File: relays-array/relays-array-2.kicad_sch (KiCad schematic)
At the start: 28 parts, among them J1 NMJ6HCD2, J10 Screw_Terminal_01x02, J14 NMJ6HCD2, J15 Screw_Terminal_01x02, J2 NMJ6HCD2, J3 Screw_Terminal_01x02, K1 G2RL-2, K2 G2RL-2, U1 OPA134

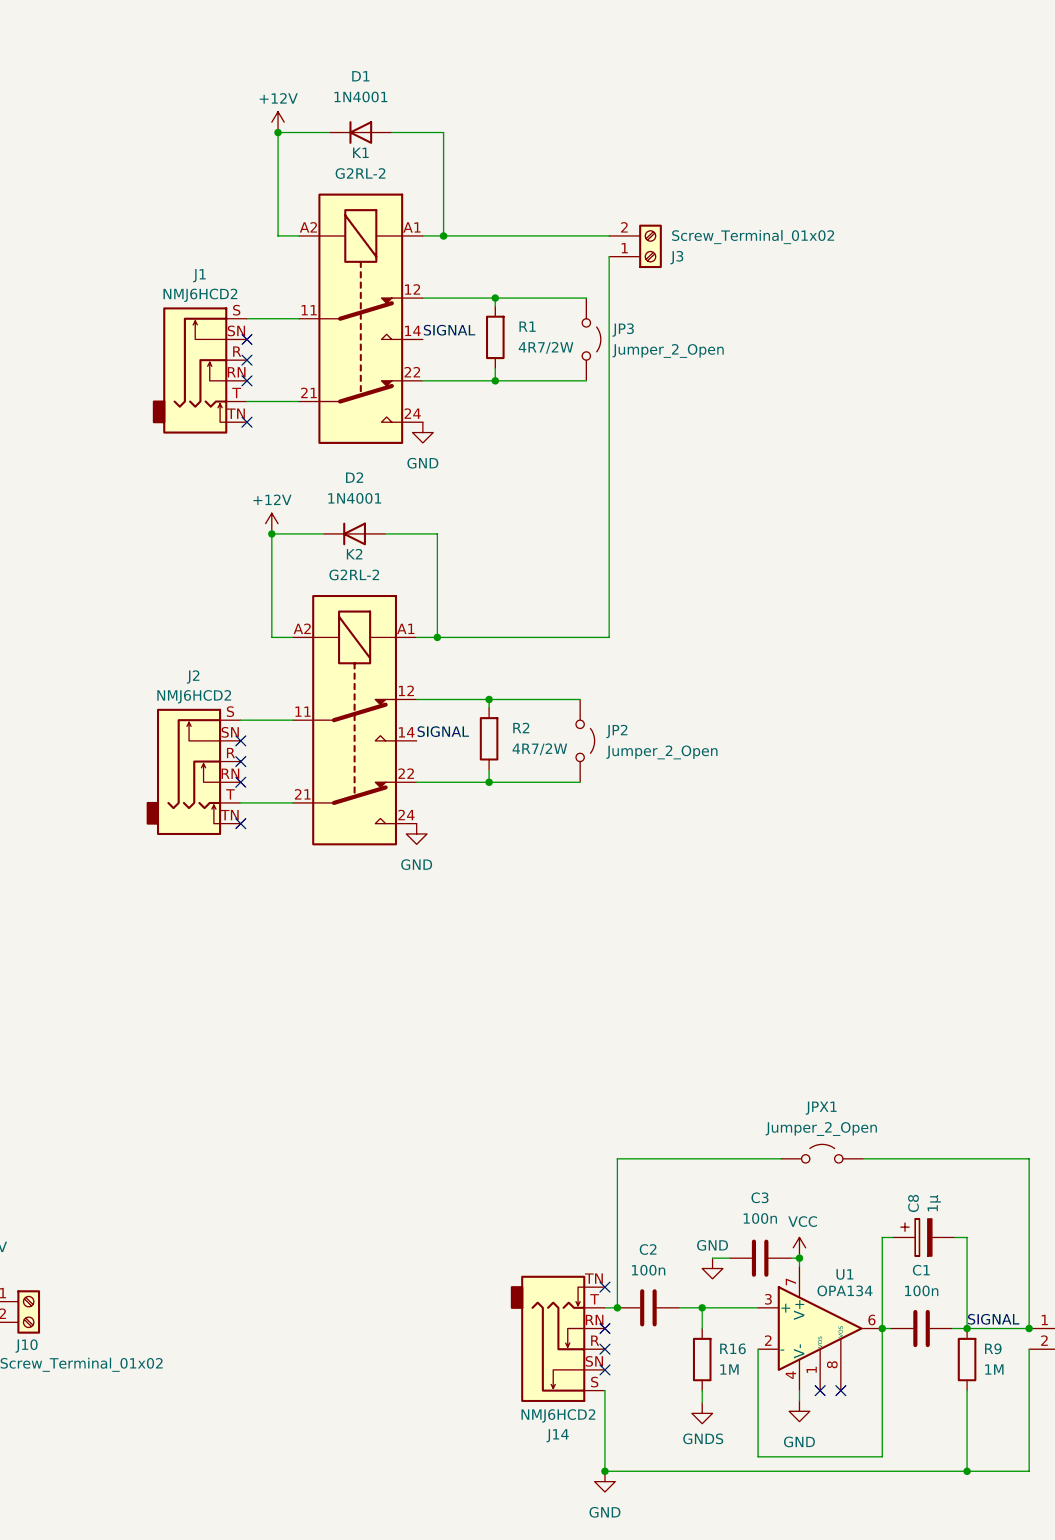
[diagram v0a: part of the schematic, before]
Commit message: relays-array: add terminal block for buffer use w/ external connector
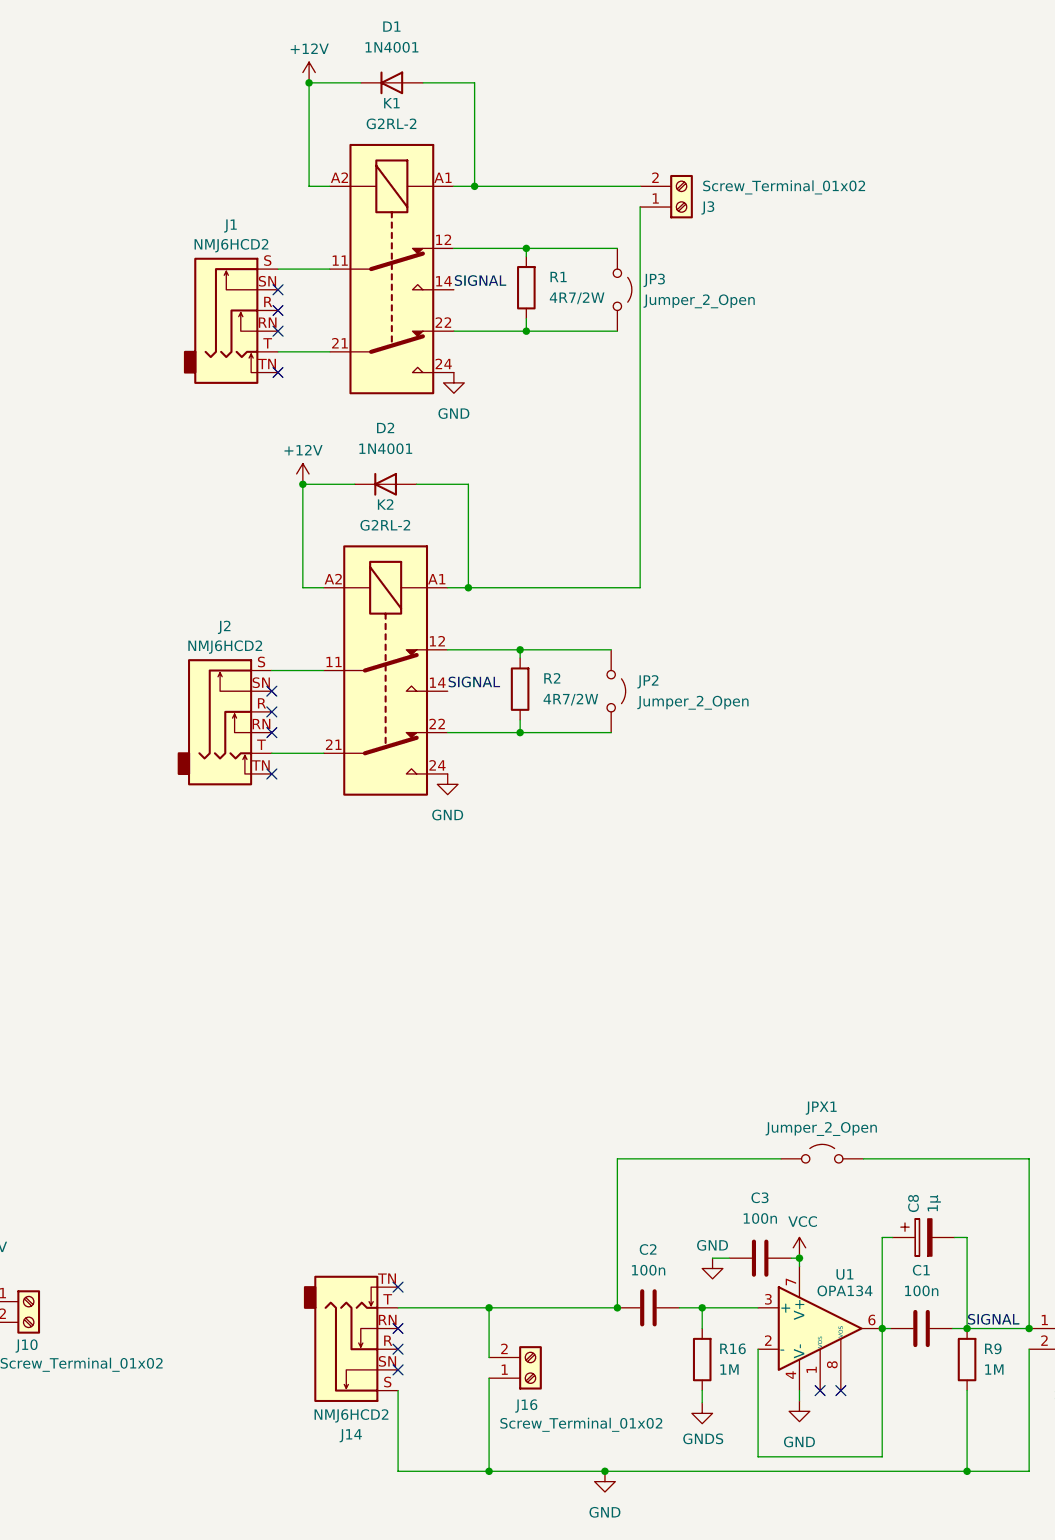
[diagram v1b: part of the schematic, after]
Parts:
- added J16: Screw_Terminal_01x02, TerminalBlock:TerminalBlock_bornier-2_P5.08mm, symbol Connector:Screw_Terminal_01x02
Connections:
- net GND: now also J16.1 (Pin_1)
- net at C2.2, J14.T, JPX1.2 (B): now also J16.2 (Pin_2)
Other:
- moved on the sheet: D1, D2, J1, J14, J2, J3, JP2, JP3, K1, K2, R1, R2

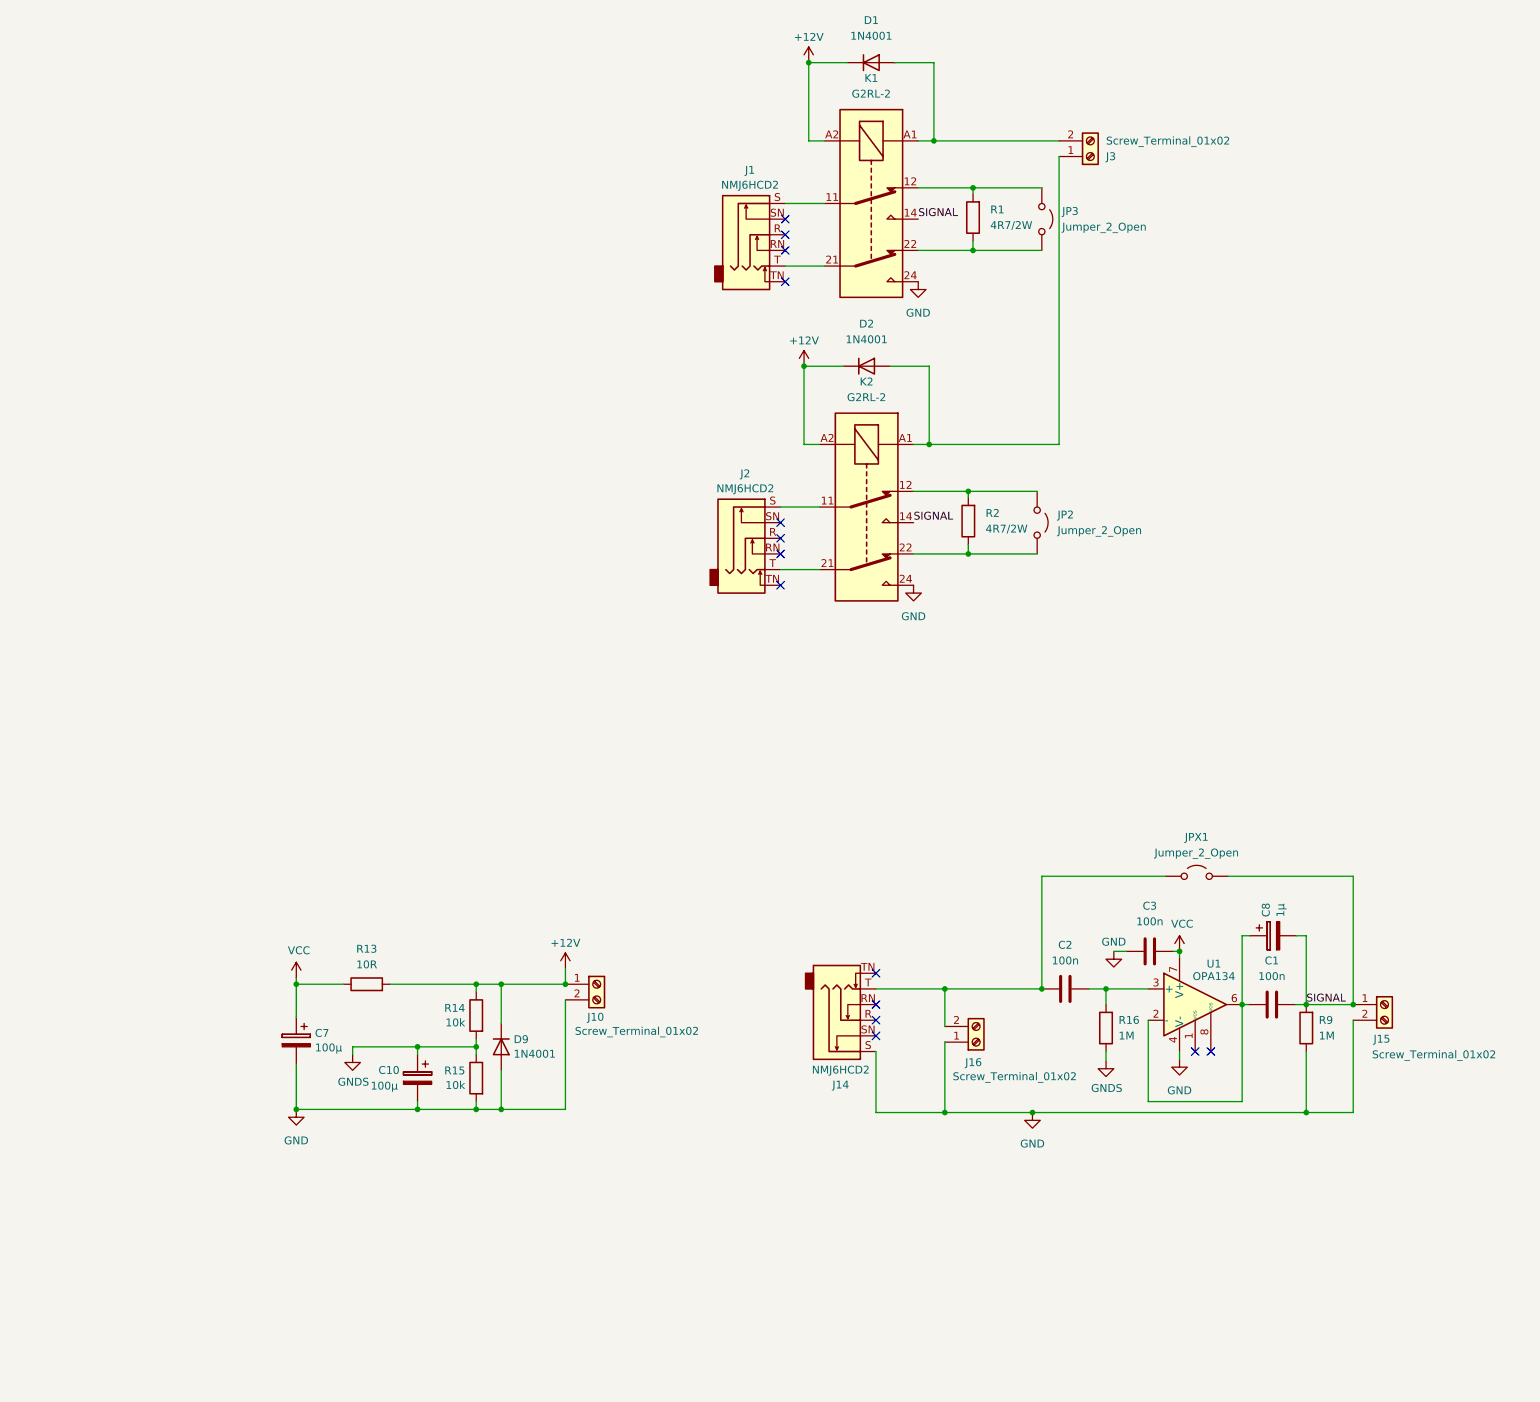
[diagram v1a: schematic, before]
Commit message: relays-array: fix schematics error and add ground plane
The jack connectors are all (except for the buffer input) wired
backwards, with the tip going to `GND` and the sleeve on `SIGNAL`, while
it should be the other way around.

While at it, improve a bit the PCB tracks and add a ground plane. The
latter is only connected to `GND` in a single point in order to avoid
ground loops and other unpleasant issues.
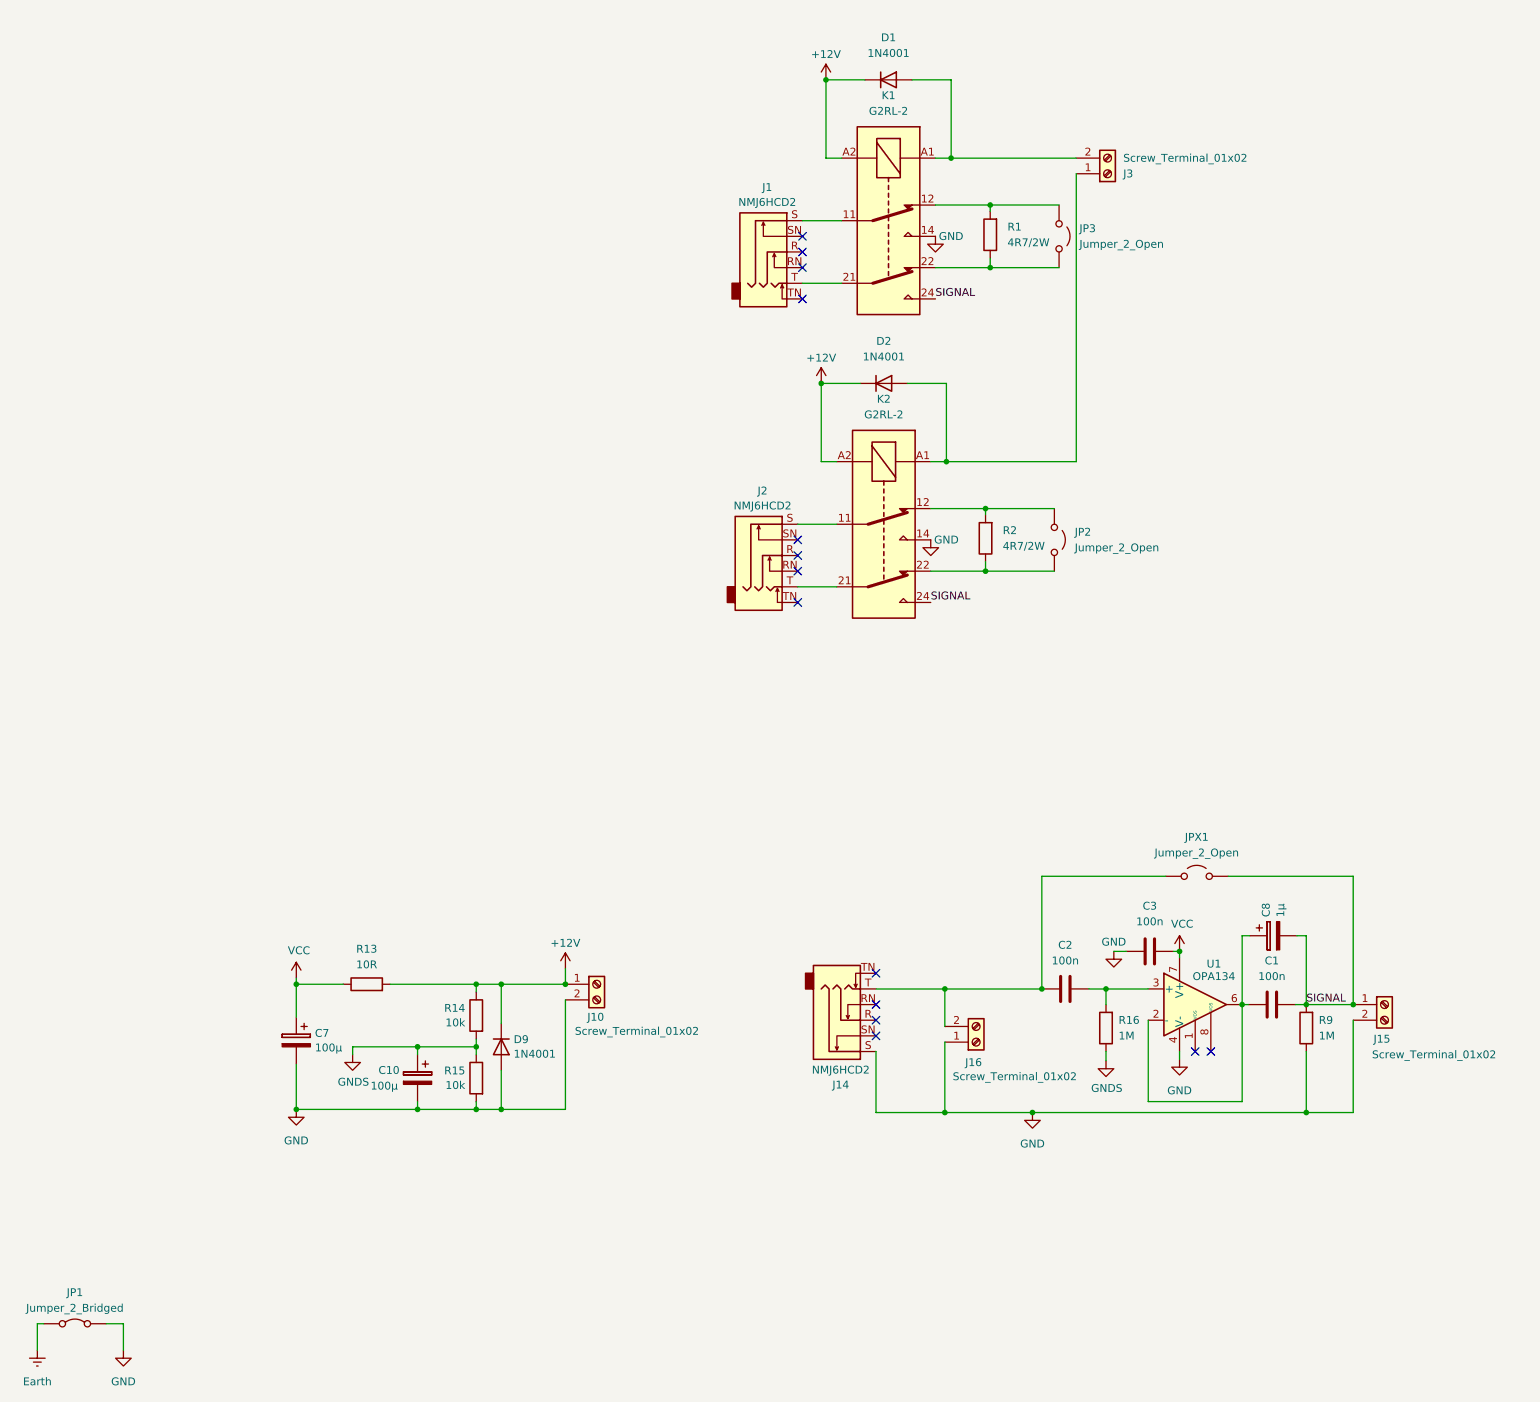
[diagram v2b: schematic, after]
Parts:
- added JP1: Jumper_2_Bridged, Jumper:SolderJumper-2_P1.3mm_Bridged_RoundedPad1.0x1.5mm, symbol Jumper:Jumper_2_Bridged
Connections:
- net GND: now also K1.14, K2.14, JP1.2 (B); no longer K1.24, K2.24
- net SIGNAL: now also K1.24, K2.24; no longer K1.14, K2.14
- new net Earth: JP1.1 (A)
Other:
- moved on the sheet: D1, D2, J1, J2, J3, JP2, JP3, K1, K2, R1, R2
